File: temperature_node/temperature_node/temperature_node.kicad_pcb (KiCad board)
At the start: 4 copper layers, 23 x 31.3 mm, 36 parts, among them J1 USB_C_Receptacle_USB2.0_16P, J2 S2B-PH-K-S, U1 ESP32-C3-WROOM-02, U2 SHT40-AD1B-R3, U3 MCP73831-2-OT, U4 USBLC6-2P6, U5 MIC5504-3.3YM5

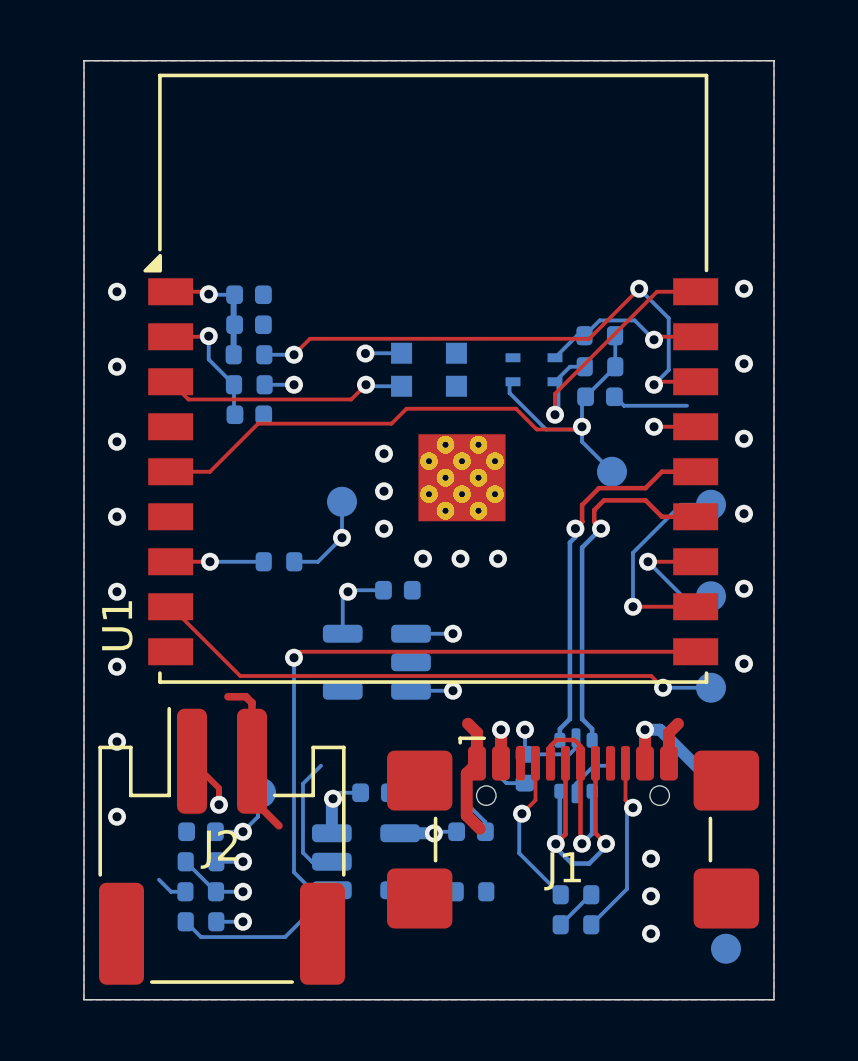
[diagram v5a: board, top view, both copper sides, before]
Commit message: update PCB with changed footprints
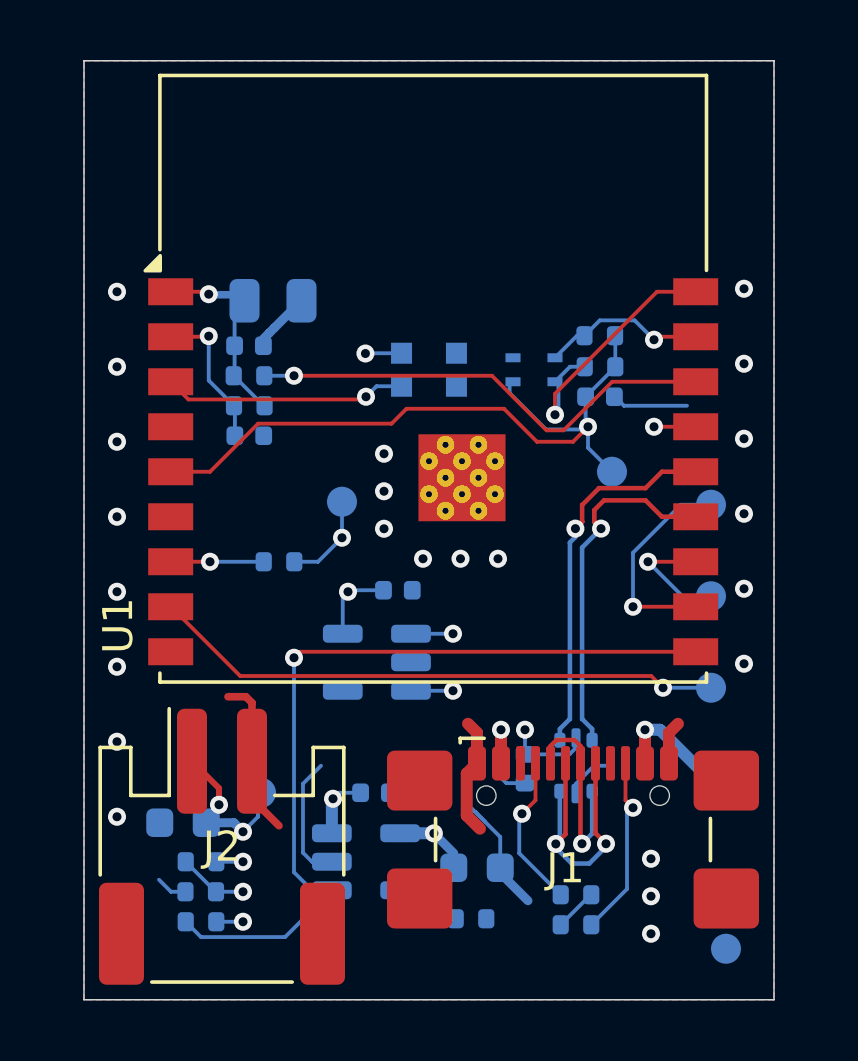
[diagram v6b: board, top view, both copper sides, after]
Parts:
- C4: footprint Capacitor_SMD:C_0402_1005Metric -> Capacitor_SMD:C_0805_2012Metric
- C6, C9: footprint Capacitor_SMD:C_0402_1005Metric -> Capacitor_SMD:C_0603_1608Metric
- J2: value S2B-PH-K-S -> S2B-PH-SM4-TB
- moved C9 1.22 mm to (134.1, 100.1)
- moved R5 0.90 mm to (133.9, 101.8)
- moved C4 0.82 mm to (127.3, 81.2)
- moved C2 0.70 mm to (126.5, 85.7)
- moved C3 0.70 mm to (126.5, 82.7)
- moved R2 0.70 mm to (126.5, 84.7)
- moved R3 0.70 mm to (126.5, 83.7)
- moved C6 0.67 mm to (124.3, 98.6)
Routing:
- net GND: track 23.9 -> 29.3 mm
- net Net-(U1-IO2): track 18.6 -> 15.8 mm, vias 3 -> 1
- net +3.3V: track 12.2 -> 13.3 mm, vias 5 -> 4
- net +BATT: track 11.2 -> 12.1 mm
- net VBUS: track 9.99 -> 10.7 mm
- net /EN: track 4.26 -> 4.96 mm
- net /SHT_EN: track 23.7 -> 24.3 mm

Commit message: Mod F.silkscreen
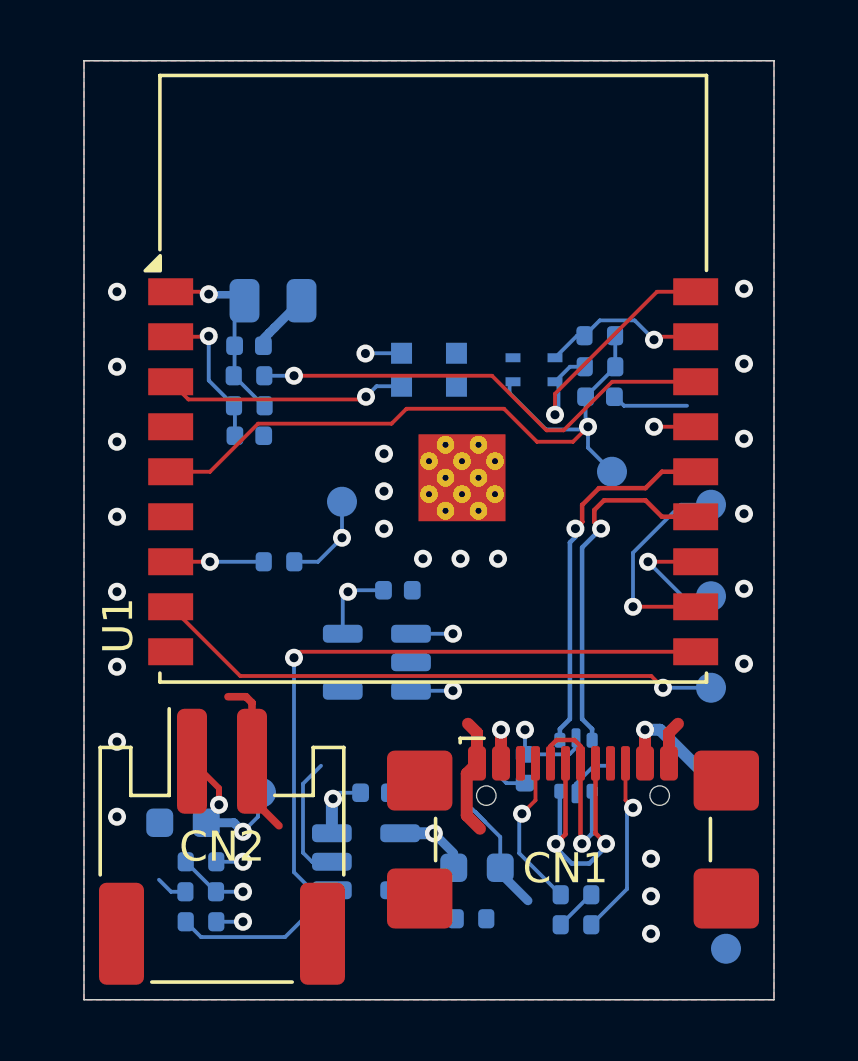
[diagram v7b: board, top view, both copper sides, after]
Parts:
- renumbered J1 to CN1, J2 to CN2
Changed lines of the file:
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@@
 		(descr "USB 2.0 Type C Receptacle, GCT, 16P, top mounted, horizontal, 5A, https://gct.co/files/drawings/usb4110.pdf")
 		(tags "USB 2.0 C Type-C Receptacle SMD 16P 16C USB4110-GF-A")
-		(property "Reference" "J1"
+		(property "Reference" "CN1"
 			(at -0.25 -0.18 0)
 			(unlocked yes)
@@
 		(descr "JST PH series connector, S2B-PH-SM4-TB (http://www.jst-mfg.com/product/pdf/eng/ePH.pdf), generated with kicad-footprint-generator")
 		(tags "connector JST PH horizontal")
-		(property "Reference" "J2"
+		(property "Reference" "CN2"
 			(at 0 0 0)
 			(layer "F.SilkS")
